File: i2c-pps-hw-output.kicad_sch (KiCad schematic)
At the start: 0 parts

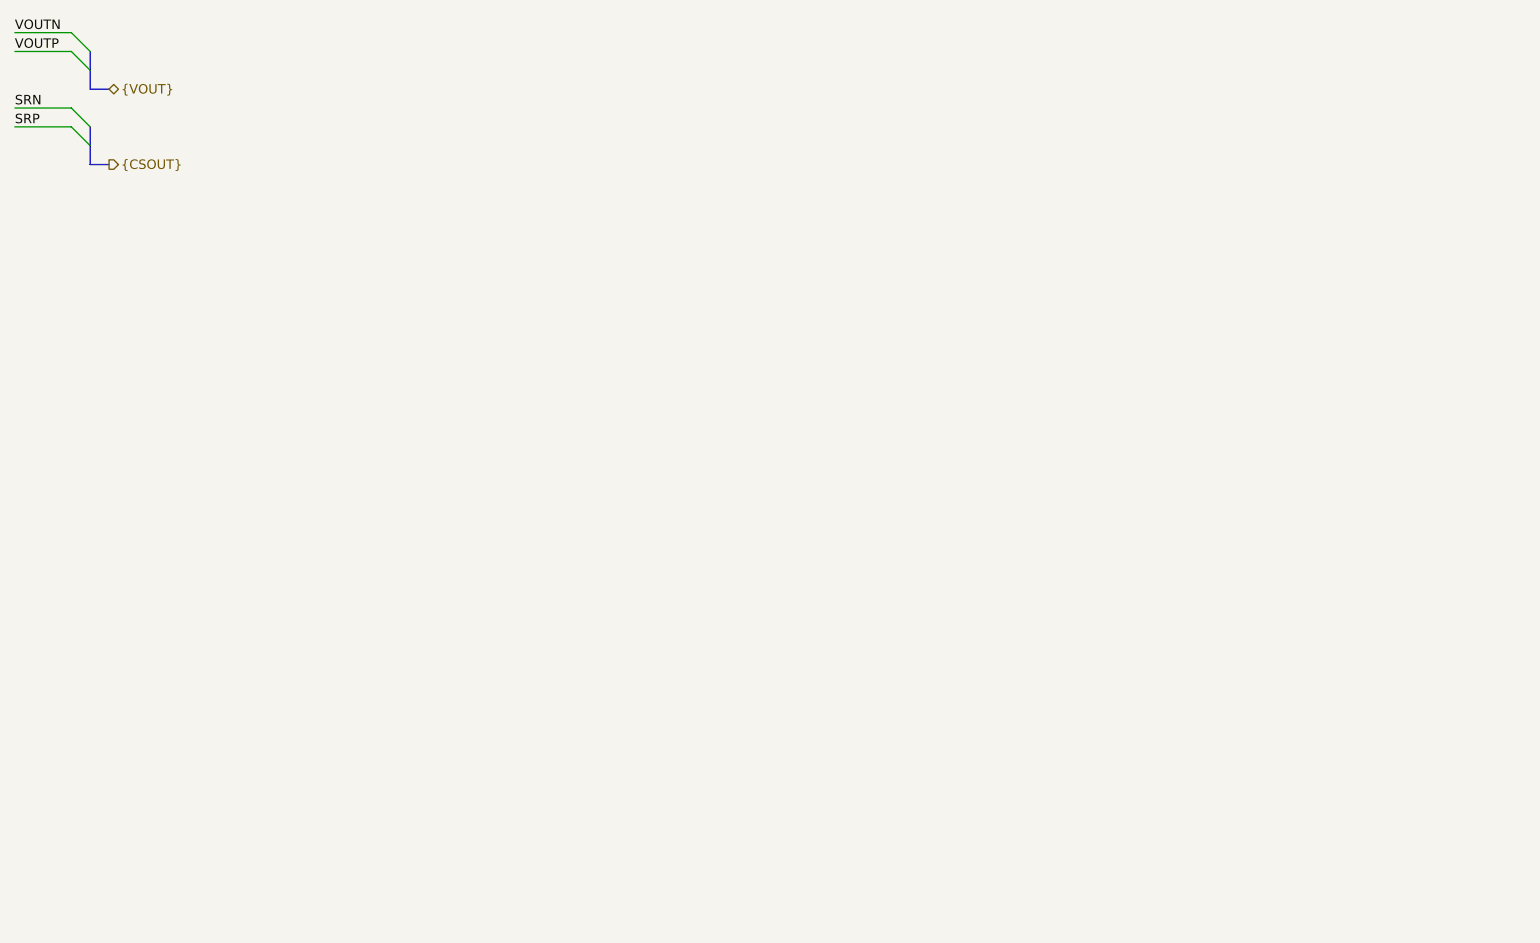
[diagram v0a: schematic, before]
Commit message: Design schematics and set per component requirements
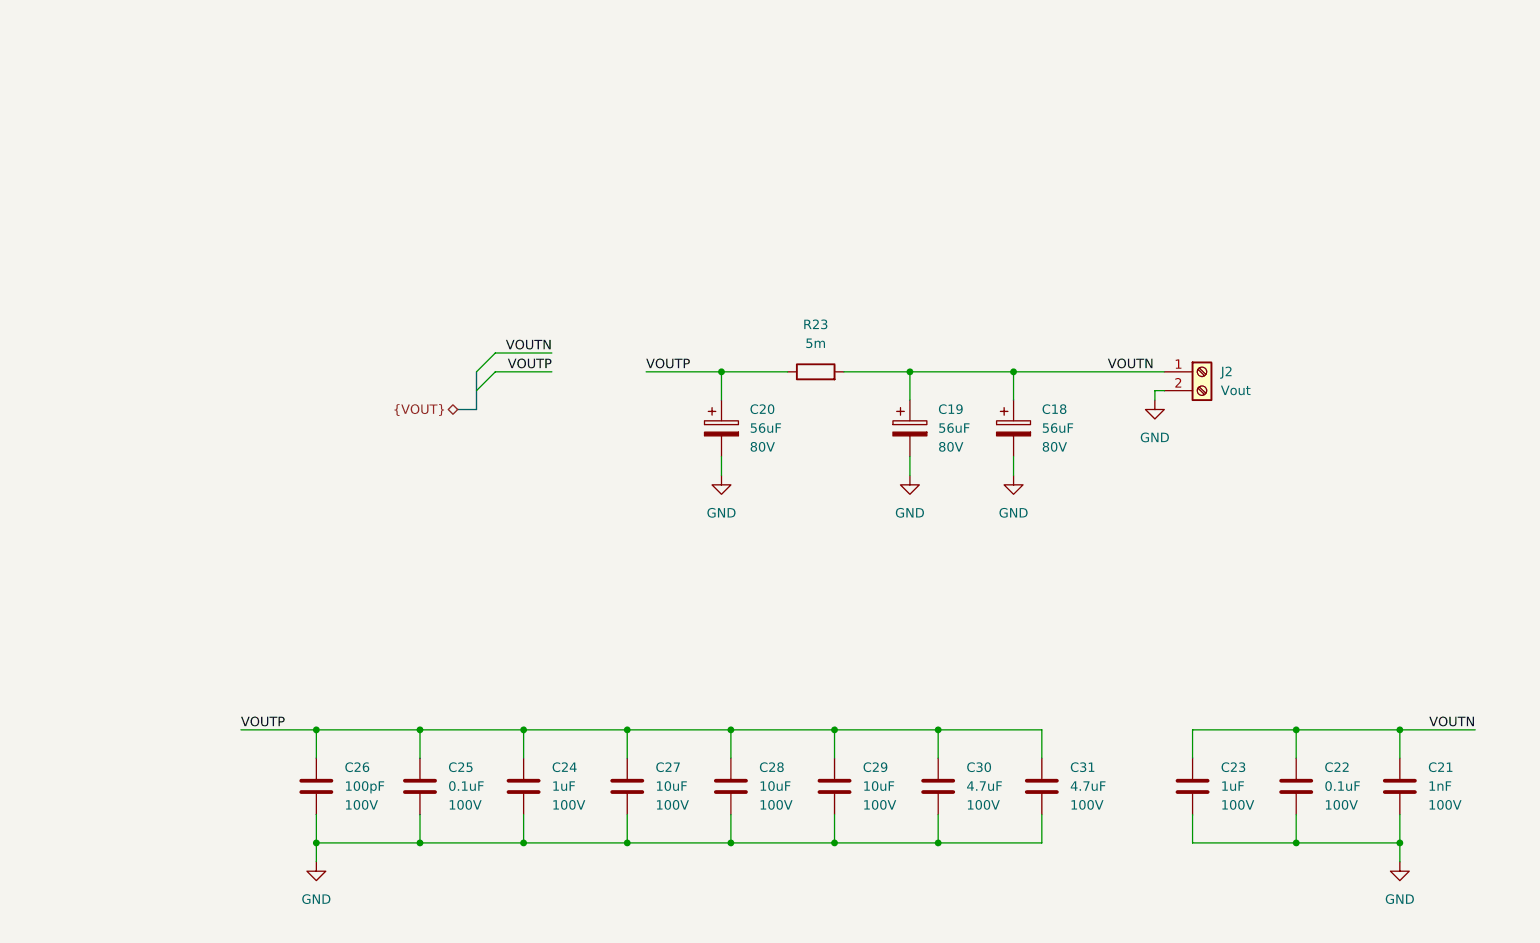
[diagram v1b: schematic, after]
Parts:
- added C18, C19, C20: 56uF, Capacitor_SMD:C_Elec_10x10.2, symbol Device:C_Polarized
- added C21: 1nF, Capacitor_SMD:C_0603_1608Metric_Pad1.08x0.95mm_HandSolder, symbol Device:C
- added C22, C25: 0.1uF, Capacitor_SMD:C_0603_1608Metric_Pad1.08x0.95mm_HandSolder, symbol Device:C
- added C23, C24: 1uF, Capacitor_SMD:C_0805_2012Metric, symbol Device:C
- added C26: 100pF, Capacitor_SMD:C_0603_1608Metric_Pad1.08x0.95mm_HandSolder, symbol Device:C
- added C27, C28, C29: 10uF, Capacitor_SMD:C_1210_3225Metric, symbol Device:C
- added C30, C31: 4.7uF, Capacitor_SMD:C_1210_3225Metric, symbol Device:C
- added J2: Vout, symbol Connector:Screw_Terminal_01x02
- added R23: 5m, Resistor_SMD:R_1206_3216Metric, symbol Device:R
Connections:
- net VOUTN: now also C18.1, C19.1, C21.1, C22.1, C23.1, J2.1 (Pin_1), R23.2
- net VOUTP: now also C20.1, C24.1, C25.1, C26.1, C27.1, C28.1, C29.1, C30.1, C31.1, R23.1
- new net GND: C18.2, C19.2, C20.2, C21.2, C22.2, C23.2, C24.2, C25.2, C26.2, C27.2, C28.2, C29.2, C30.2, C31.2, J2.2 (Pin_2)

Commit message: Rename VOUTP to VOUT_Switcher for clarity
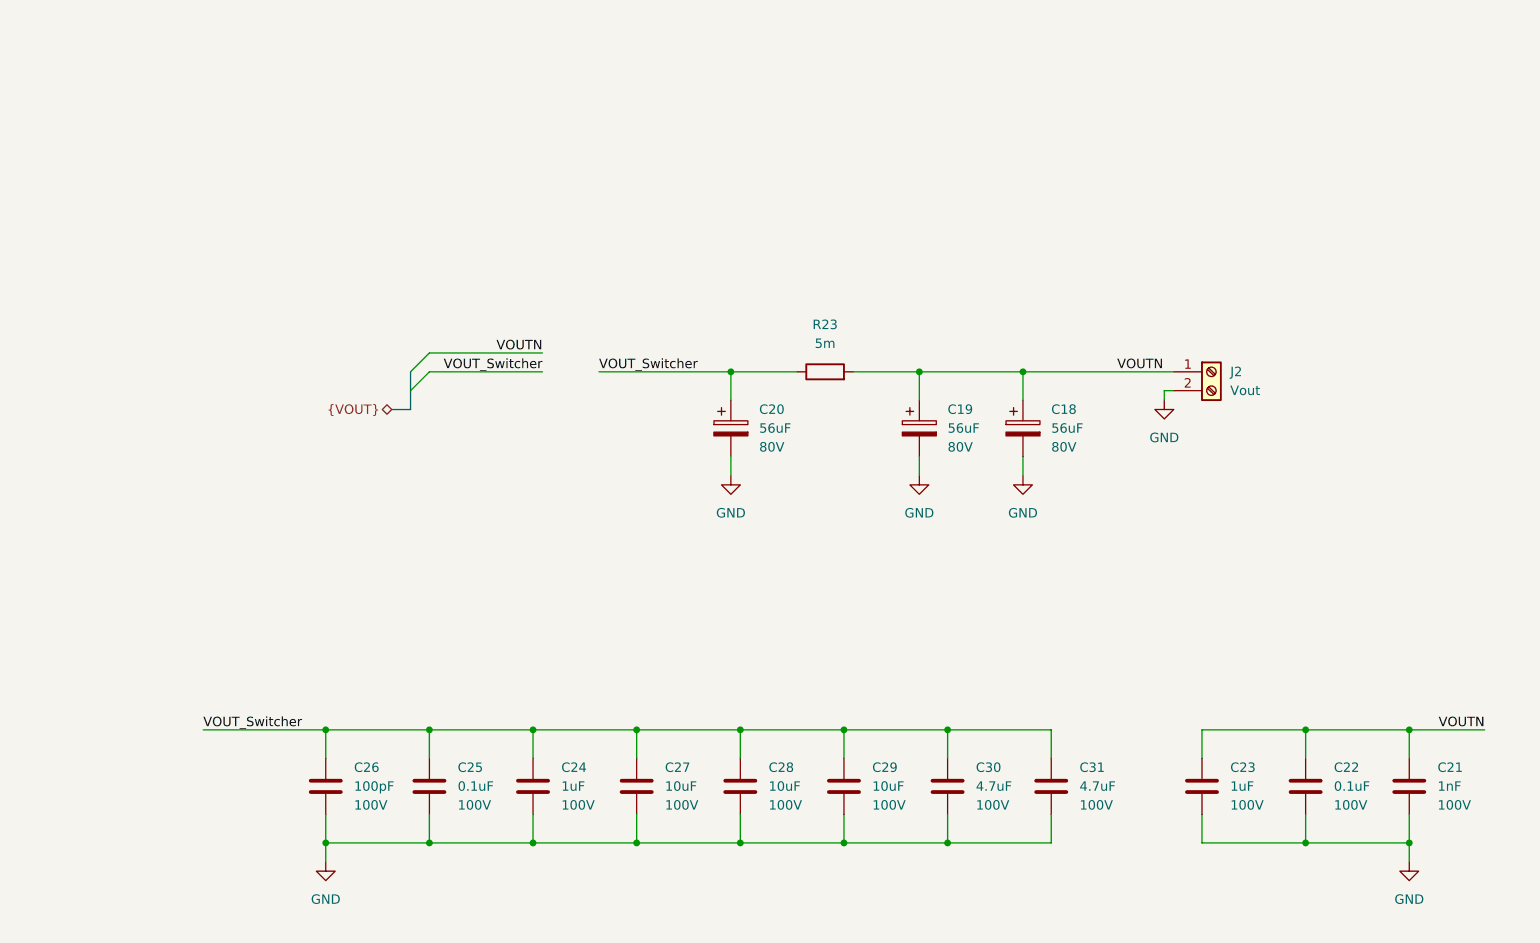
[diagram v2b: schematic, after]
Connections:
- net VOUTP renamed VOUT_Switcher
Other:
- moved on the sheet: C18, C19, C20, C21, C22, C23, C24, C25, C26, C27, C28, C29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

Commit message: Rename VOUTN to VOUT_Filtered for clarity
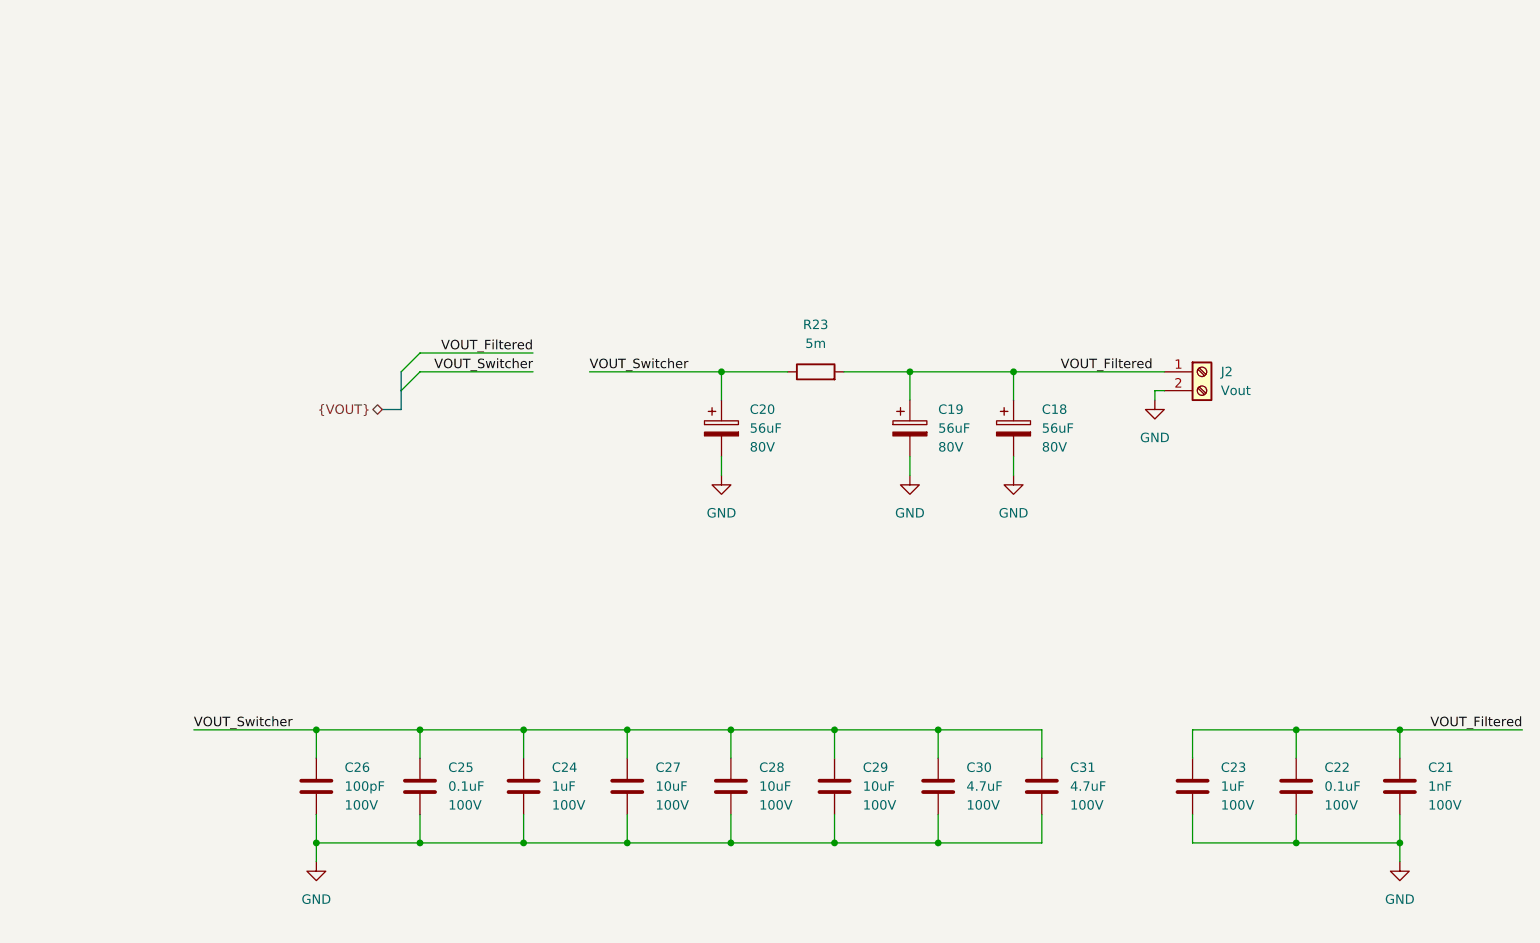
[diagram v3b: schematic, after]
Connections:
- net VOUTN renamed VOUT_Filtered
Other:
- moved on the sheet: C18, C19, C20, C21, C22, C23, C24, C25, C26, C27, C28, C29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

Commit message: Add more indicator LEDs
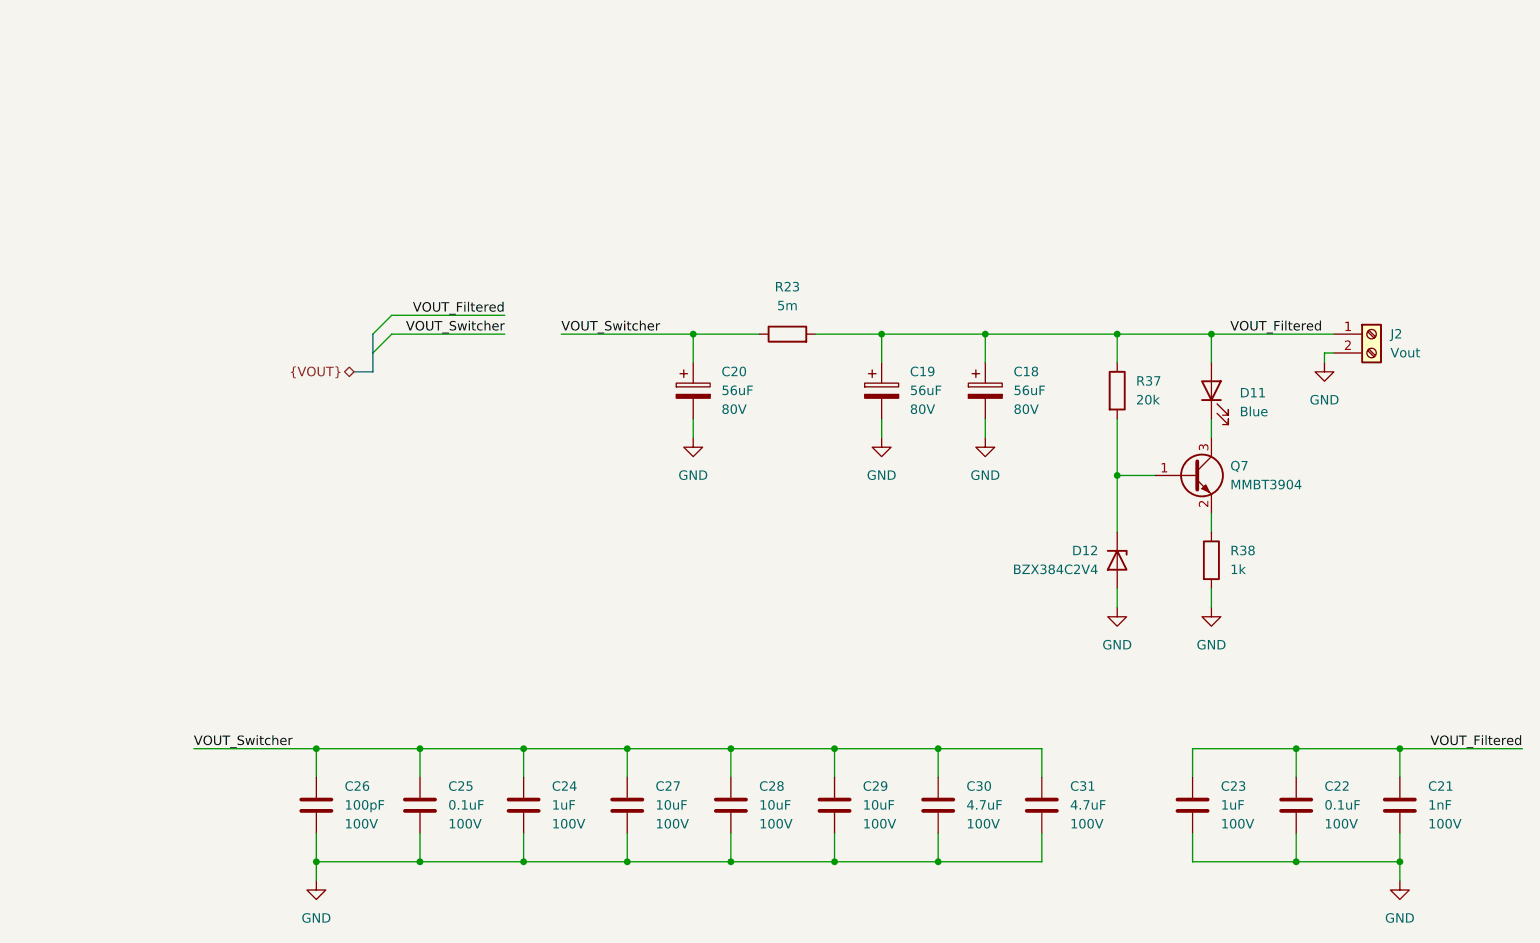
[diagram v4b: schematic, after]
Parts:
- added D11: Blue, LED_SMD:LED_0603_1608Metric_Pad1.05x0.95mm_HandSolder, symbol Device:LED
- added D12: BZX384C2V4, Diode_SMD:D_SOD-323, symbol Device:D_Zener
- added Q7: MMBT3904, Package_TO_SOT_SMD:SOT-23, symbol Transistor_BJT:MMBT3904
- added R37: 20k, Resistor_SMD:R_0603_1608Metric_Pad0.98x0.95mm_HandSolder, symbol Device:R
- added R38: 1k, Resistor_SMD:R_0603_1608Metric_Pad0.98x0.95mm_HandSolder, symbol Device:R
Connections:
- net GND: now also D12.2 (A), R38.2
- net VOUT_Filtered: now also D11.2 (A), R37.1
- new net: D12.1 (K), Q7.1 (B), R37.2
- new net: D11.1 (K), Q7.3 (C)
- new net: Q7.2 (E), R38.1
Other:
- moved on the sheet: C18, C19, C20, C21, C22, C23, C24, C25, C26, C27, C28, C29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

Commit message: Select market available components
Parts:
- C18, C19, C20: Manufacturer (none) -> KEMET; Part Number (none) -> A768MS566M1KLAE034
- C21: Manufacturer (none) -> TDK Corporation; Part Number (none) -> CGA3E2X7R2A102K080AA
- C22, C25: Manufacturer (none) -> Taiyo Yuden; Part Number (none) -> HMK107B7104KAHT
- C23, C24: Manufacturer (none) -> KYOCERA AVX; Part Number (none) -> 08051C105K4Z2A
- C26: Manufacturer (none) -> TDK Corporation; Part Number (none) -> CGA3E2C0G2A101J080AA
- C27, C28, C29: Manufacturer (none) -> TDK Corporation; Part Number (none) -> C3225X7R2A106K250AC
- C30, C31: Manufacturer (none) -> Murata Electronics; Part Number (none) -> GCJ32DC72A475KE01L
- D11: Manufacturer (none) -> Lite-On Inc; Part Number (none) -> LTST-C193TBKT-5A
- D12: Manufacturer (none) -> Vishay General Semiconductor - Diodes Division; Part Number (none) -> BZX384C2V4-E3-08
- J2: footprint (none) -> TerminalBlock_MetzConnect:TerminalBlock_MetzConnect_Type101_RT01602HBWC_1x02_P5.08mm_Horizontal
- Q7: Manufacturer (none) -> MCC (Micro Commercial Components); Part Number (none) -> MMBT3904-TP
- R23: footprint Resistor_SMD:R_1206_3216Metric -> Resistor_SMD:R_2512_6332Metric; Manufacturer (none) -> YAGEO; Part Number (none) -> PA2512FKM070R005E
- R37: Manufacturer (none) -> YAGEO; Part Number (none) -> RC0603JR-0720KL
- R38: Manufacturer (none) -> YAGEO; Part Number (none) -> RC0603JR-071KL
